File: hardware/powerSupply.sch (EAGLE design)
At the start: 52 parts, among them IC1 MCP3008, IC2 LM334Z, IC3 MCP4821P, IC4 MCP4821P, J1 1X2-3.5MM, J2 1X2-3.5MM, J3 RASPBERRYPI-40-PIN-GPIO_PTH, T1 2N3904, T2 2N3904, U1 LM358, U2 LM358, U3 MAX874CPA

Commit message: 
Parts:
- added C10, C12: 100n, adafruit:C-US050-024X044
- added C11: 2.2u, rcl:CPOL-USE5-6
- added IC5: 74LS139D, 74xx-us:74LS139D
- added JP1, JP2: (no value), adafruit:PINHD-1X3
- added R28, R29: 10R, rcl:R-US_0204/7
- added U4: LM358, SparkFun-IC-Amplifiers:LM358
- added U5: (no value), Hexellence-mixedSignal:INA219
- C1: value (none) -> 220u 25V; device adafruit:C-US050-024X044 -> rcl:CPOL-USE5-6
- C2, C4, C5, C7, C8, C9: value (none) -> 100n
- C3, C6: value (none) -> 2.2u; device adafruit:C-US050-024X044 -> rcl:CPOL-USE5-6
- D1, D2: value (none) -> 1N5821
- R1, R21: value (none) -> 100R; device SparkFun-Resistors:RESISTORAXIAL-0.3 -> rcl:R-US_0204/7
- R10, R11, R2, R3, R4, R5, R6, R7, R8, R9: value (none) -> 10R; device SparkFun-Resistors:RESISTORAXIAL-0.3 -> rcl:R-US_0204/7
- R12, R13, R14, R15, R19, R20, R26, R27: value (none) -> 18K 0.1%; device SparkFun-Resistors:RESISTORAXIAL-0.3 -> rcl:R-US_0204/7
- R16, R17: value (none) -> 1K; device SparkFun-Resistors:RESISTORAXIAL-0.3 -> rcl:R-US_0204/7
- R18, R25: value (none) -> 1K 0.1%; device SparkFun-Resistors:RESISTORAXIAL-0.3 -> rcl:R-US_0204/7
- R22, R23: value (none) -> 10K; device SparkFun-Resistors:RESISTORAXIAL-0.3 -> rcl:R-US_0204/7
- R24: value (none) -> 470R; device SparkFun-Resistors:RESISTORAXIAL-0.3 -> rcl:R-US_0204/7
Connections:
- net N$3 renamed 4.096V
- removed net A0: J3.RXI
- removed net A1: J3.TXO
- new net CS4: IC5B.Y3
- new net CS5: IC5B.Y2
- new net CS6: IC5B.Y1
- new net CS7: IC5B.Y0
- new net LCD_CS: IC5A.Y3
- new net N$19: R28.2, U5.VIN-
- new net N$20: JP1.2, R22.1, R23.1
- new net N$21: U5.SCL
- new net N$23: IC5A.A, IC5B.A
- new net N$24: IC5A.B, IC5B.B
- new net SDA: U5.SDA
- new net V+1: C4.1, D1.C, R10.2, R11.2, R2.2, R28.1, R3.2, R4.2, R5.2, R6.2, R7.2, R8.2, R9.2, U$1.VIN, U1G1.+IN, U4G3.P$V+
- net 3.3V: now also C10.1, C12.1, C8.1, C9.1, IC3.SHDN, IC3.VDD, IC4.SHDN, IC4.VDD
- net 5V: now also C2.1, U5.VCC; no longer C8.1, C9.1, IC3.SHDN, IC3.VDD, IC4.SHDN, IC4.VDD
- net ADC_CS: now also IC5A.Y0
- net ADC_IOUT: now also C6.+; no longer C2.1
- net GND: now also C1.-, C10.2, C11.-, C12.2, C3.-, C6.-, JP1.3, R14.1, U4G3.P$V-, U5.A0, U5.A1, U5.GND; no longer C1.2, C3.2, C6.2, R14.2, U1G3.P$V-
- net IDAC_CS: now also IC5A.Y2
- net MISO: no longer J3.MISO
- net MOSI: no longer J3.MOSI
- net N$14: now also JP1.1; no longer R22.1, R23.1
- net N$4: now also R29.1, U5.VIN+; no longer D1.C, R10.2, R11.2, R2.2, R3.2, R4.2, R5.2, R6.2, R7.2, R8.2, R9.2, U$1.VIN, U1G1.+IN
- net N$9: now also R14.2; no longer R14.1
- net OE0: now also IC5A.G; no longer J3.CE0
- net OE1: now also IC5B.G; no longer J3.CE1
- net SCLK: no longer J3.SCLK
- net V+: now also C1.+, R29.2; no longer C3.1, C4.1, U1G3.P$V+
- net VADJ: now also C3.+; no longer C6.1
- net VDAC_CS: now also IC5A.Y1
- net VOUT: now also C11.+; no longer C1.1
- net VOUT_ADC: now also IC1.CH0
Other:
- note added: "10x10R <1% 1V->1A"
- note added: "JP1 jumper setting will disable current limiting."
- moved on the sheet: C2, C4, C5, C7, C8, C9, D1, D2, IC1, IC2, IC3, IC4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

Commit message: 
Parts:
- removed JP2: (no value), adafruit:PINHD-1X3
- added C13: 100n, adafruit:C-US050-024X044
- added LCD1: LCD-16X2SILK, Hexellence-Displays:LCD-16X2SILK
- added TM1: (no value), adafruit:TRIMPOTTC33X
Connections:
- net N$23 renamed A0
- net N$24 renamed A1
- removed net N$21: U5.SCL
- removed net SDA: U5.SDA
- new net N$18: LCD1.A, TM1.E
- new net N$3: LCD1.VO, TM1.S
- new net RS: LCD1.RS
- net 5V: now also C13.1, LCD1.VDD, TM1.A
- net GND: now also C13.2, LCD1.K, LCD1.VSS
- net LCD_CS: now also LCD1.CS
- net MOSI: now also LCD1.SDI
- net SCLK: now also LCD1.SCLK
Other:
- moved on the sheet: J3

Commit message: 
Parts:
- removed J3: RASPBERRYPI-40-PIN-GPIO_PTH, SparkFun-Connectors:RASPBERRYPI-40-PIN-GPIO_PTH
- added C14, C15, C16, C17: 100n, adafruit:C-US050-024X044
- added J4: RASPBERRYPI-40-PIN-GPIO_PTH, Hexellence-Connectors:RASPBERRYPI-40-PIN-GPIO_PTH
- added R30, R31, R32, R33, R34, R35, R36, R37: 10K, rcl:R-US_0204/7
- added SW1, SW3: EC12E_SW, switch-alps:EC12E_SW
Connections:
- removed net RS: LCD1.RS
- new net N$21: J4.GP26, LCD1.RS
- new net N$22: R30.1, R32.2, SW1G$1.B
- new net N$23: C14.1, J4.GP19, R30.2
- new net N$24: C15.1, J4.GP16, R34.2
- new net N$25: R34.1, R36.2, SW1G$1.A
- new net N$26: C16.1, J4.GP20, R31.2
- new net N$27: C17.1, J4.GP21, R35.2
- new net N$28: R31.1, R33.2, SW3G$1.B
- new net N$29: R35.1, R37.2, SW3G$1.A
- net 3.3V: now also J4.3.3V@1, J4.3.3V@17; no longer J3.3.3V
- net 5V: now also J4.5V@2, J4.5V@4, R32.1, R33.1, R36.1, R37.1; no longer J3.5V
- net A0: now also J4.GP6
- net A1: now also J4.GP5
- net CS7: now also IC4.SDI
- net GND: now also C14.2, C15.2, C16.2, C17.2, J4.GND@14, J4.GND@20, J4.GND@25, J4.GND@30, J4.GND@34, J4.GND@39, J4.GND@6, J4.GND@9, SW1G$1.C, SW3G$1.C
- net MISO: now also J4.MISO
- net MOSI: now also J4.MOSI; no longer IC4.SDI
- net OE0: now also J4.CE0
- net OE1: now also J4.CE1
- net SCLK: now also J4.SCLK
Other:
- moved on the sheet: C3

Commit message: 
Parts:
- added SW2: EC11B_SW, Hexellence-Switch:EC11B_SW
- added SW4, SW5, SW6: (no value), adafruit:SWITCH_PUSHBUTTONEVQ-PE
- SW1: value EC12E_SW -> EC11B_SW; device switch-alps:EC12E_SW -> Hexellence-Switch:EC11B_SW
- SW3: value EC12E_SW -> (none); device switch-alps:EC12E_SW -> adafruit:SWITCH_PUSHBUTTONEVQ-PE
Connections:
- new net N$30: J4.GP23, SW3.P$1
- new net N$31: J4.GP24, SW4.P$1
- new net N$32: J4.GP25, SW5.P$1
- new net N$33: J4.GP26, SW6.P$1
- new net N$34: J4.SDA, U5.SDA
- new net N$35: J4.SCL, U5.SCL
- net GND: now also SW1G$2.G, SW1G$3.G, SW2G$1.C, SW2G$2.G, SW2G$3.G, SW3.P$2, SW4.P$2, SW5.P$2, SW6.P$2; no longer SW3G$1.C
- net N$21: now also J4.GP4; no longer J4.GP26
- net N$22: now also SW2G$1.B; no longer SW1G$1.B
- net N$25: now also SW2G$1.A; no longer SW1G$1.A
- net N$28: now also SW1G$1.A; no longer SW3G$1.B
- net N$29: now also SW1G$1.B; no longer SW3G$1.A
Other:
- moved on the sheet: SW1

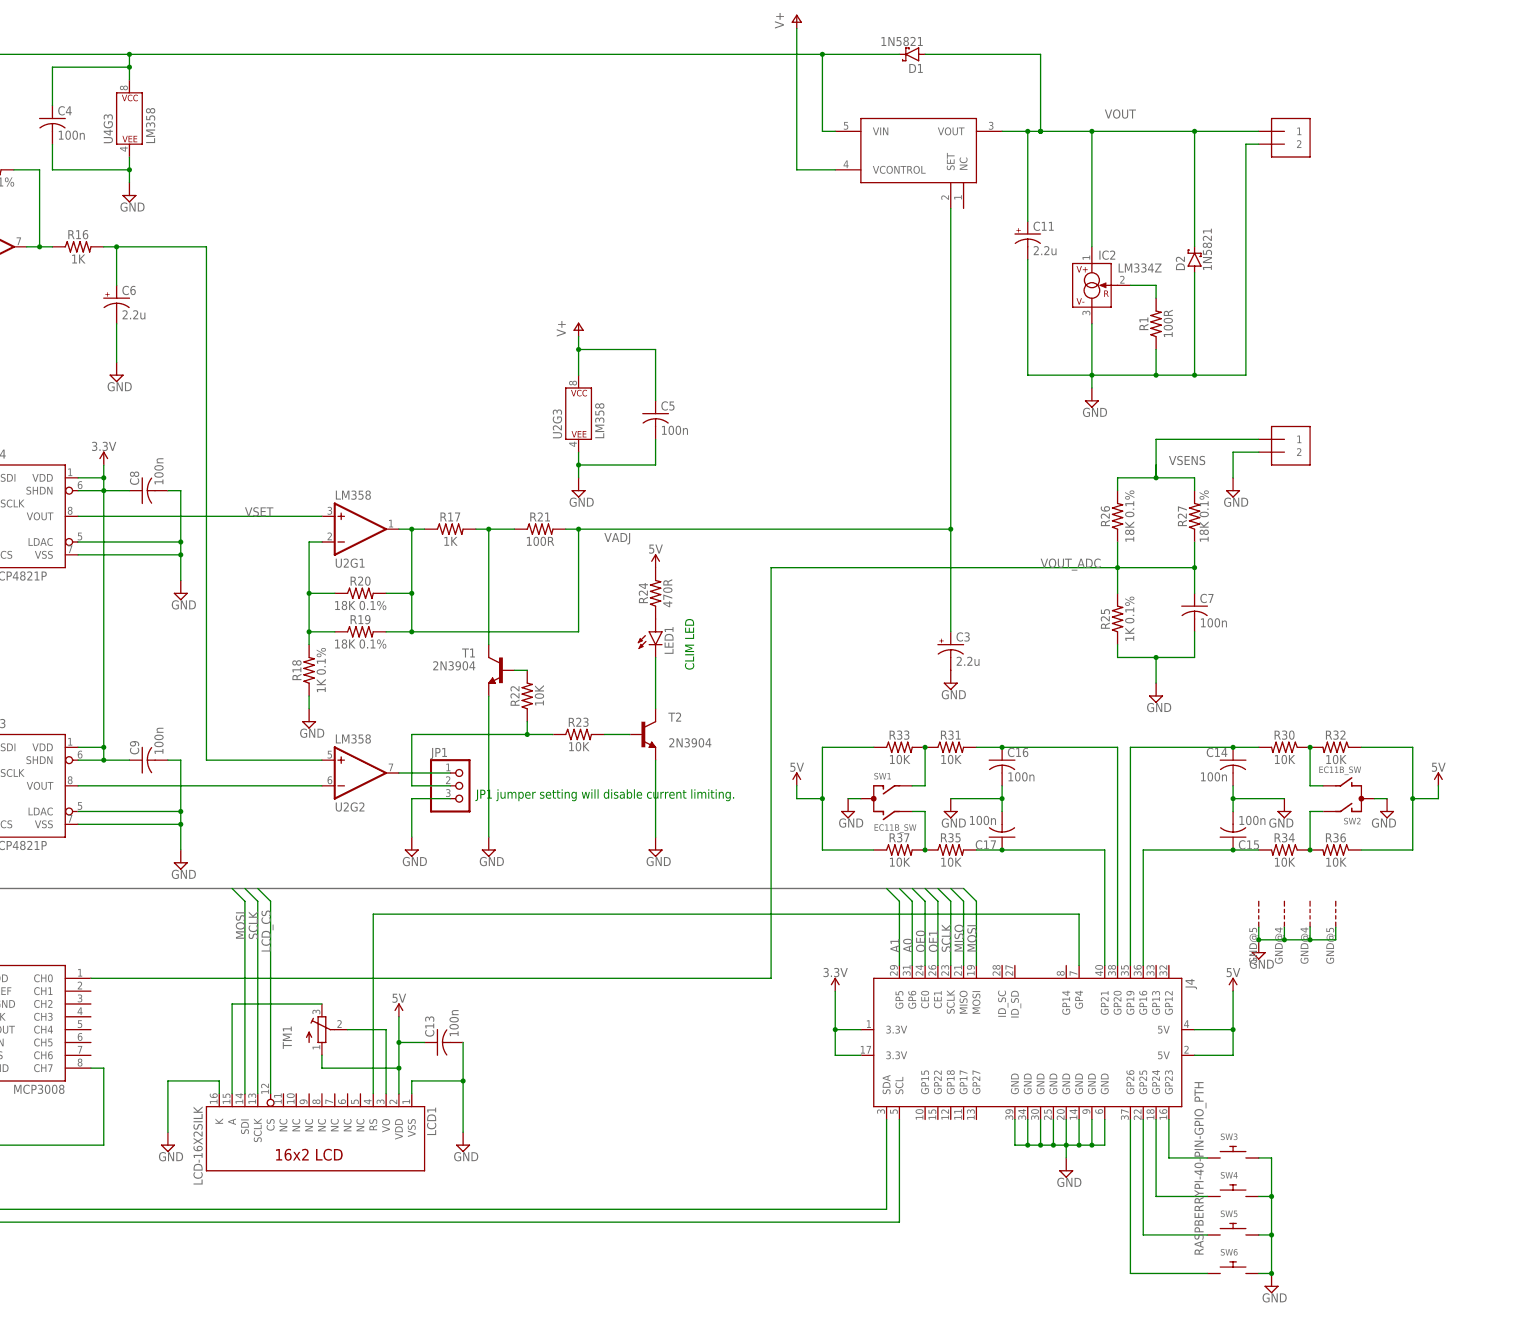
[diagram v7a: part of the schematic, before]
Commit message: 
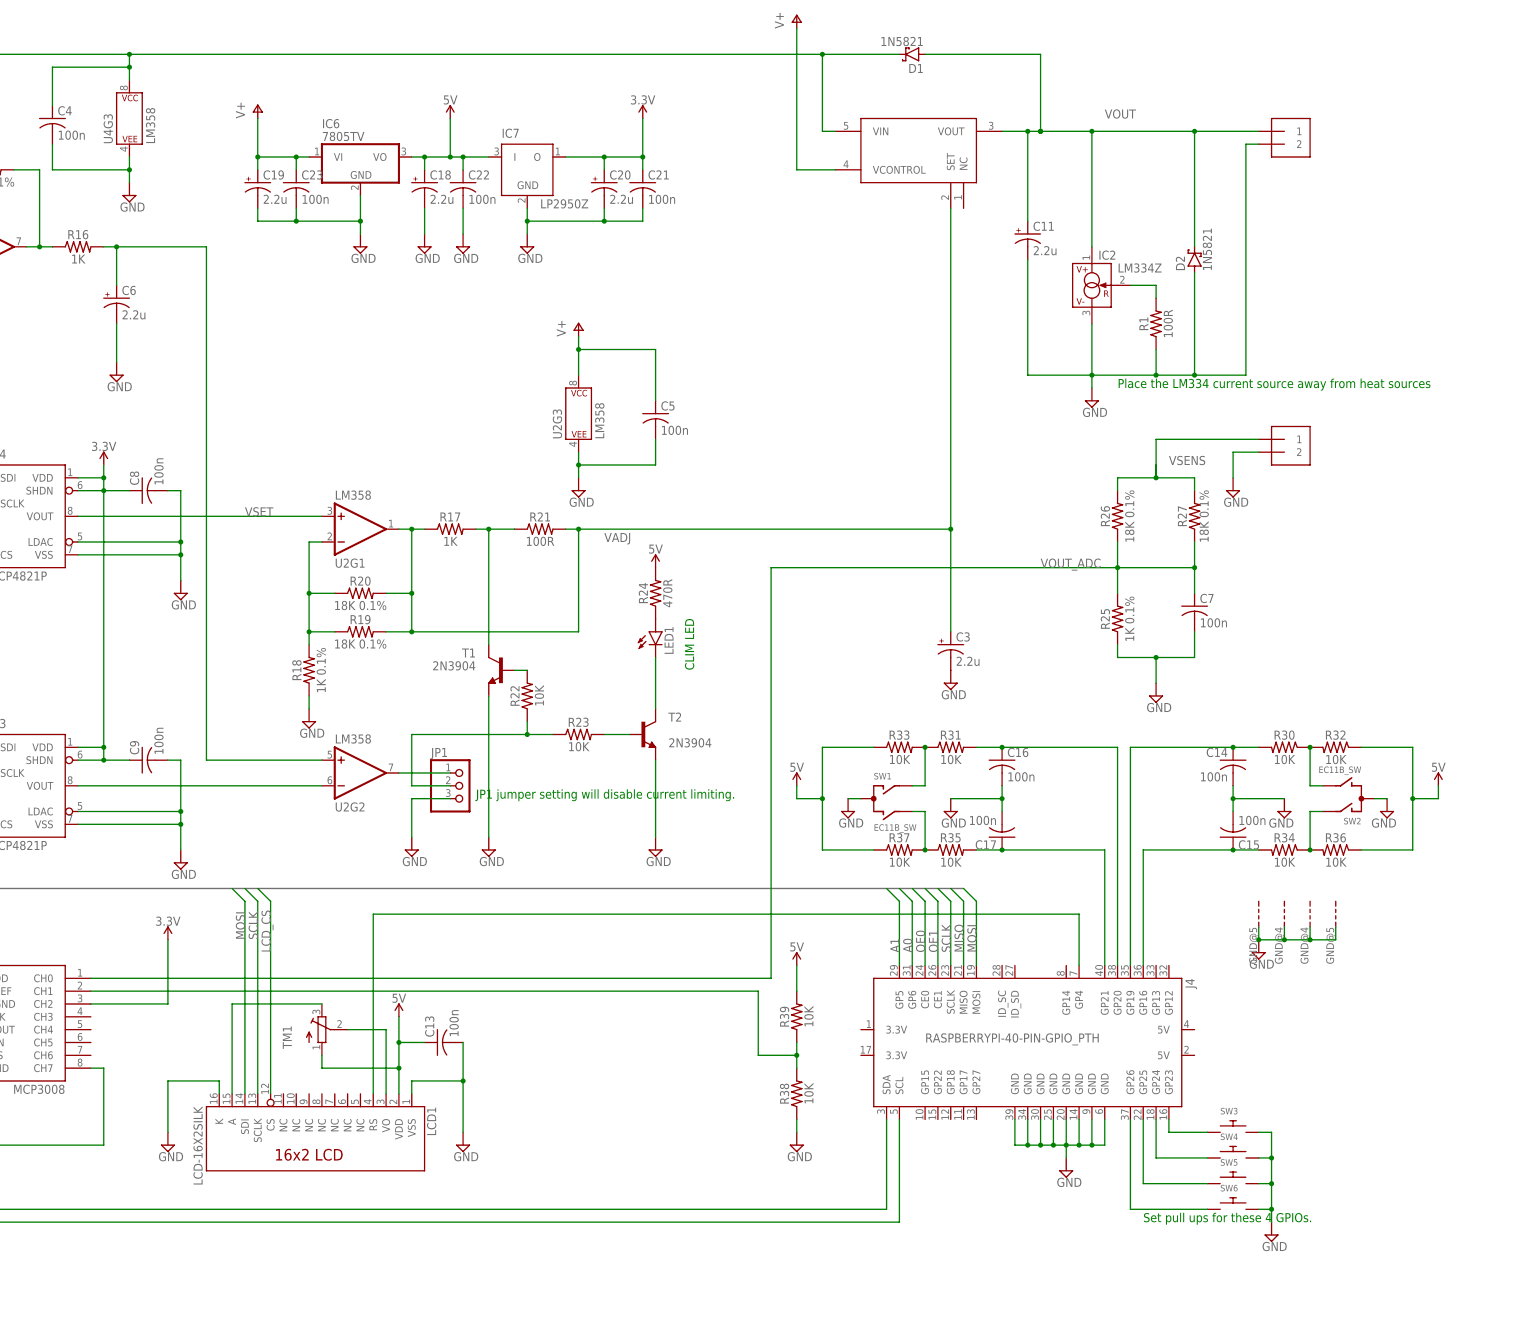
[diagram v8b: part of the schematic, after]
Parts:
- added C18, C19, C20: 2.2u, rcl:CPOL-USE5-6
- added C21, C22, C23: 100n, adafruit:C-US050-024X044
- added IC6: 7805TV, linear:7805TV
- added IC7: LP2950Z, linear:LP2950Z
- added R38, R39: 10K, rcl:R-US_0204/7
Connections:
- net N$2 renamed 0.064@25C
- new net N$2: IC1.CH1, R38.2, R39.1
- net 3.3V: now also C20.+, C21.1, IC1.CH2, IC7.O; no longer J4.3.3V@1, J4.3.3V@17
- net 5V: now also C18.+, C22.1, IC6.VO, IC7.I, R39.2; no longer J4.5V@2, J4.5V@4
- net GND: now also C18.-, C19.-, C20.-, C21.2, C22.2, C23.2, IC6.GND, IC7.GND, R38.1
- net V+: now also C19.+, C23.1, IC6.VI
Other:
- note added: "Place the LM334 current source away from heat sources"
- note added: "Set pull ups for these 4 GPIOs."
- moved on the sheet: SW3, SW4, SW5, SW6
